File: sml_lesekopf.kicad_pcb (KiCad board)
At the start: 2 copper layers, 27 x 27 mm, 28 parts, among them J1 +Ub, J2 GND, J3 TTL_IN, J4 TTL_OUT, J5 B, J6 A, J7 Z, J8 Y, Q1 BC807, Q2 SFH309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

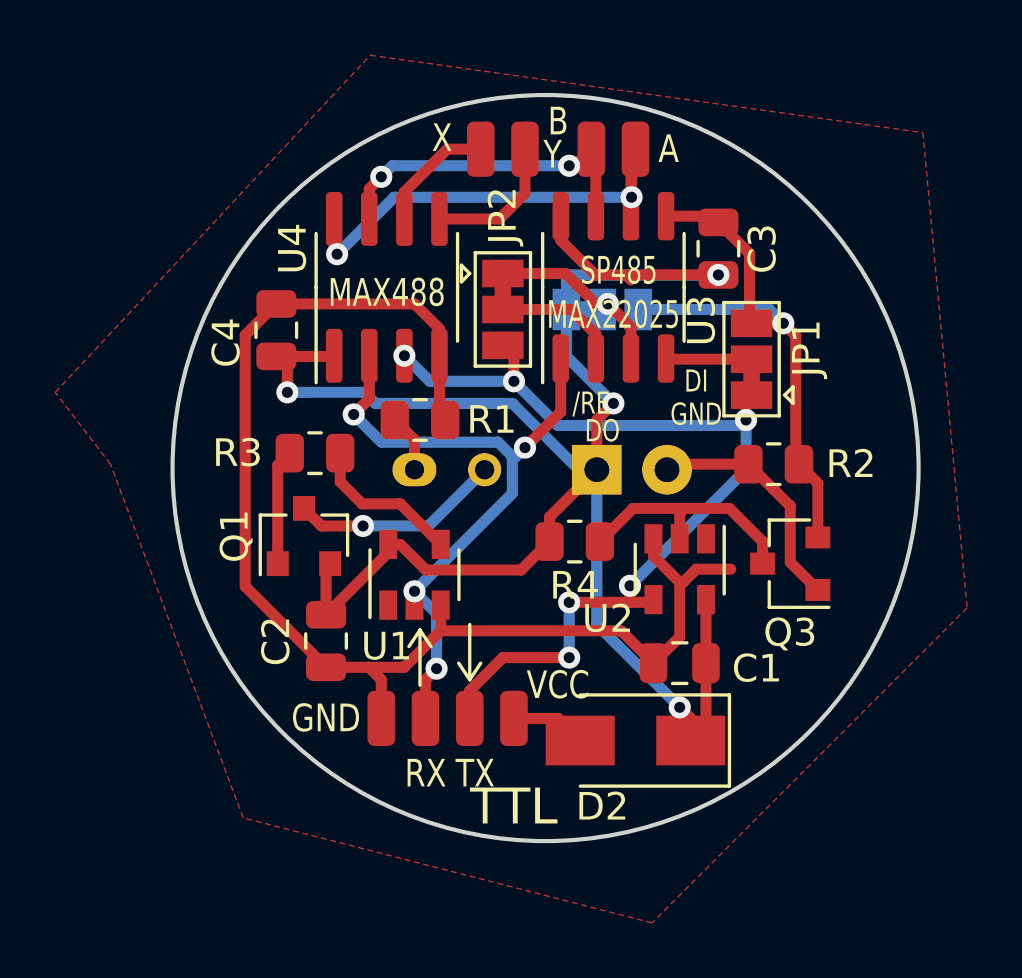
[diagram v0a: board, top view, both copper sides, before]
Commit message: update IR led
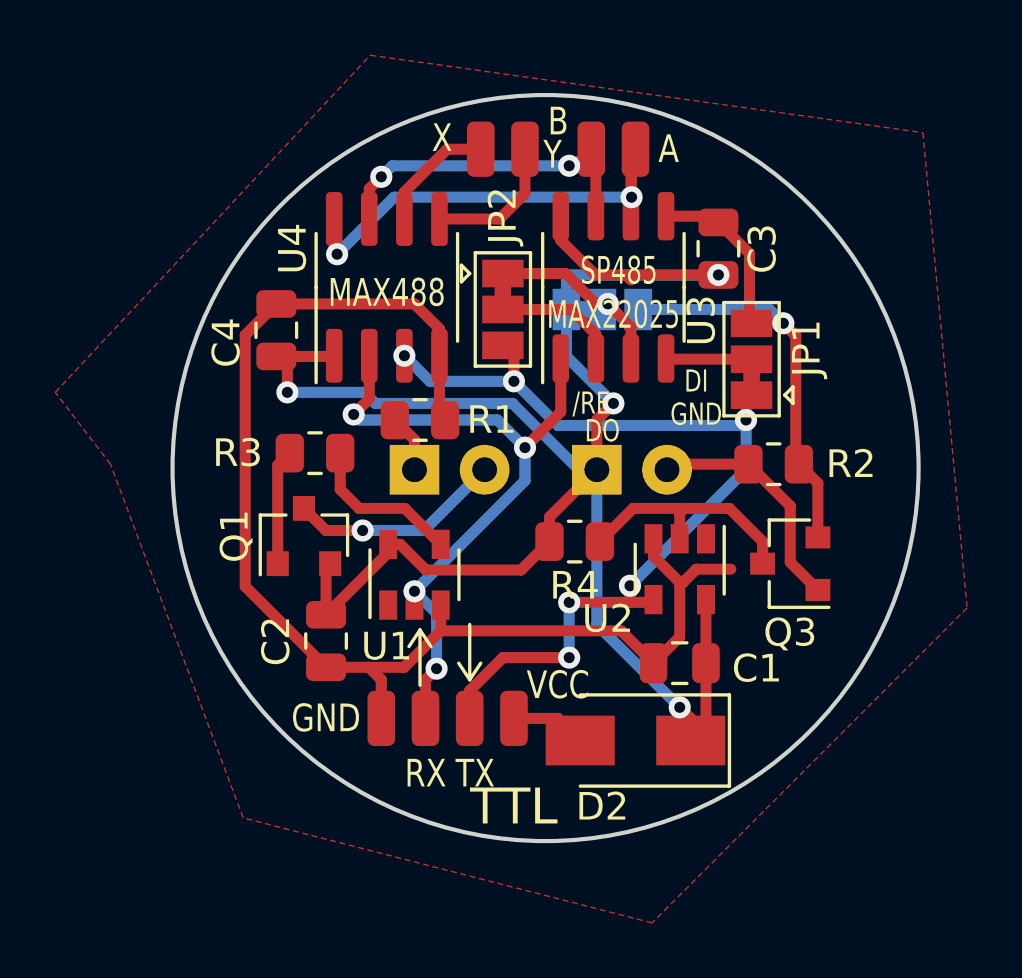
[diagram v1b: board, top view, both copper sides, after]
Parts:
- D1: footprint Package_TO_SOT_THT:TO-18-2_Window -> LED_THT:LED_D3.0mm_IRGrey
